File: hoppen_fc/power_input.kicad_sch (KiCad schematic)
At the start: 0 parts

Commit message: power input/generation reworked
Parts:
- added C54: 1u 50V, 0_capacitor_smd:C_0603_1608Metric, symbol Device:C
- added C55: 2u2, 0_capacitor_smd:C_0603_1608Metric, symbol Device:C
- added C57: 100n, 0_capacitor_smd:C_0402_1005Metric, symbol Device:C
- added D10: SMBJ51CD-M3/H, Diode_SMD:D_SMB, symbol 0_diodes:SMBJ51CD-M3/H
- added J4: XT30_MALE, 0_connectors:XT30PW-M, symbol 0_connectors:Conn_01x02_Mounting
- added Q2: NMOS, 0_transistors:DFN-8, symbol Simulation_SPICE:NMOS
- added U10: LM74700, 0_power:SOT-23-6, symbol 0_power:LM74700
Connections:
- new net: C54.2, U10.1 (VCAP)
- new net: Q2.2 (G), U10.5 (GATE)
- new net +BAT: C54.1, C57.1, D10.2 (A2), J4.2 (Pin_2), Q2.3 (S), U10.3 (EN), U10.6 (ANODE)
- new net +BAT_PROT: C55.1, Q2.1 (D), U10.4 (CATHODE)
- new net GND: C55.2, C57.2, D10.1 (A1), J4.1 (Pin_1), U10.2 (GND)
- no-connect marks 0 -> 2
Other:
- note added: "INPUT VOLTAGE MINIMUM 2S MAXIMUM 6S"
- note added: "POWER CONNECTOR AND PROTECTION"
- company: (none) -> Hoppen
- title: (none) -> Power Input

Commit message: finished routing, starting doublechecking and componenting
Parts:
- removed C55: 2u2, 0_capacitor_smd:C_0603_1608Metric, symbol Device:C
- added C64, C65, C66: 10u, 0_capacitor_smd:C_0805_2012Metric, symbol Device:C
- C54: value 1u 50V -> 1u
- Q2: LCSC (none) -> C467174
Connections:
- net +BAT_PROT: now also C64.1, C65.1, C66.1
- net GND: now also C64.2, C65.2, C66.2

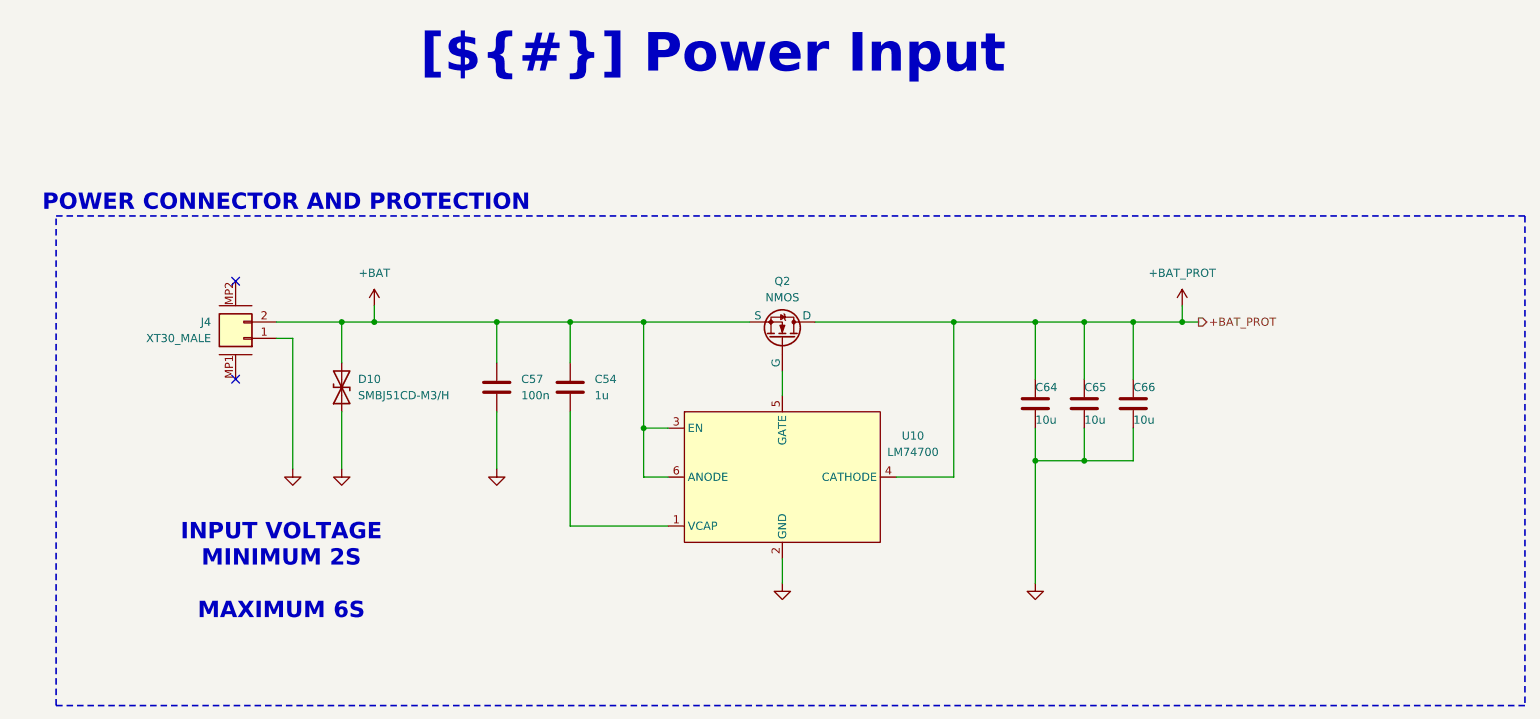
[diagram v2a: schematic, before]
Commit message: finished adding lcsc numbers
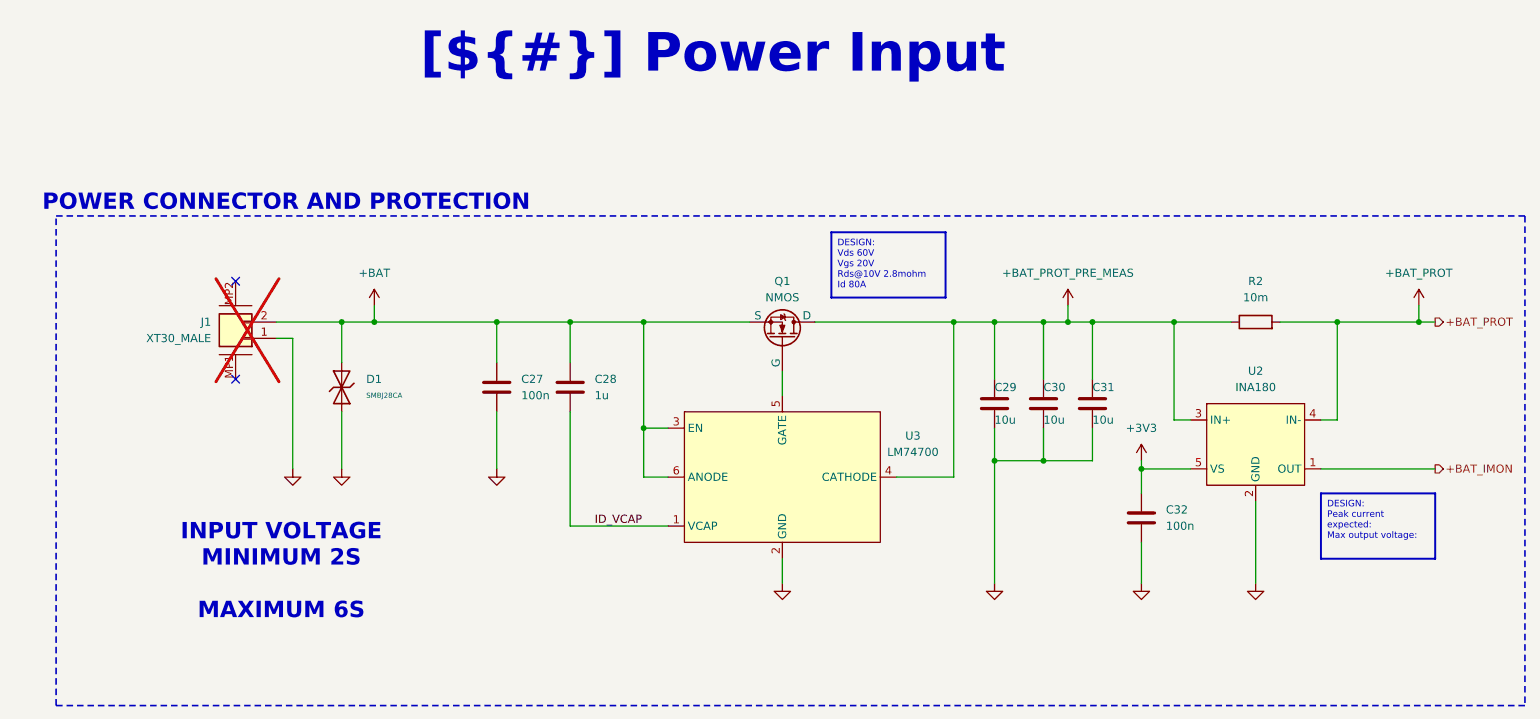
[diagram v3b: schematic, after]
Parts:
- removed D10: SMBJ51CD-M3/H, Diode_SMD:D_SMB, symbol 0_diodes:SMBJ51CD-M3/H
- added C32: 100n, 0_capacitor_smd:C_0402_1005Metric, symbol Device:C
- added D1: SMBJ28CA, PCM_JLCPCB:D_SMB, symbol PCM_JLCPCB-Diodes:TVS-Bi,SMBJ28CA
- added R2: 10m, Resistor_SMD:R_1206_3216Metric, symbol Device:R
- added U2: INA180, Package_TO_SOT_SMD:SOT-23-5, symbol 0_power:INA180
- C27: renamed from C57; LCSC (none) -> C307331
- C28: renamed from C54; LCSC (none) -> C15849
- J1: renamed from J4; now not fitted; now left out of the parts list
- renumbered C64 to C29, C65 to C30, C66 to C31, Q2 to Q1, U10 to U3
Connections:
- net +BAT: now also D1.2
- net +BAT_PROT: now also R2.2, U2.4 (IN-); no longer C29.1, C30.1, C31.1, Q1.1 (D), U3.4 (CATHODE)
- net GND: now also C32.2, D1.1, U2.2 (GND)
- net ID_VCAP: now reaches C28.2, U3.1 (VCAP)
- new net +3V3: C32.1, U2.5 (VS)
- new net +BAT_IMON: U2.1 (OUT)
- new net +BAT_PROT_PRE_MEAS: C29.1, C30.1, C31.1, Q1.1 (D), R2.1, U2.3 (IN+), U3.4 (CATHODE)
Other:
- moved on the sheet: C29, C30, C31

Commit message: ready for routing?
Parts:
- J1: now fitted
- U2: footprint Package_TO_SOT_SMD:SOT-23-5 -> 0_transceivers:SOT-23-5
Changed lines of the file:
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@@
 			)
 		)
-		(property "Footprint" "Package_TO_SOT_SMD:SOT-23-5"
+		(property "Footprint" "0_transceivers:SOT-23-5"
 			(at 224.79 60.96 0)
 			(effects
@@
 		(in_bom no)
 		(on_board yes)
-		(dnp yes)
+		(dnp no)
 		(fields_autoplaced yes)
 		(property "Reference" "J1"

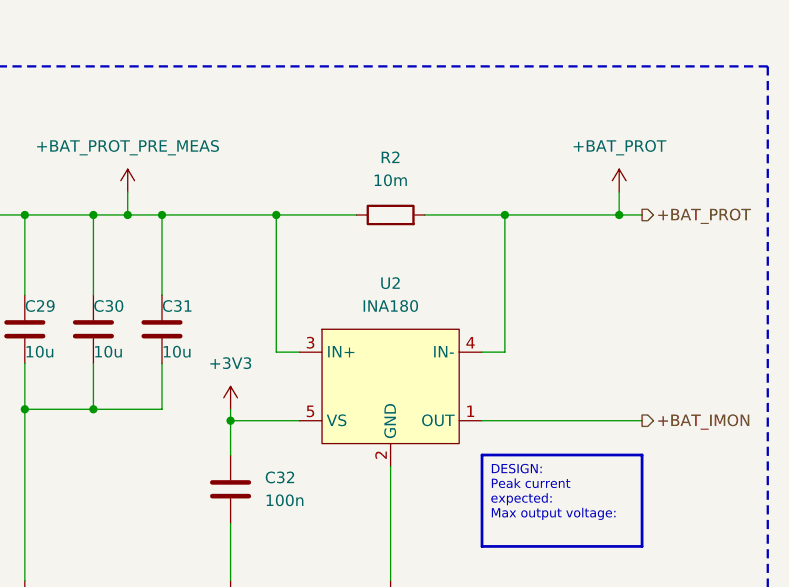
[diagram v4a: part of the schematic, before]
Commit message: routing and adding rf module
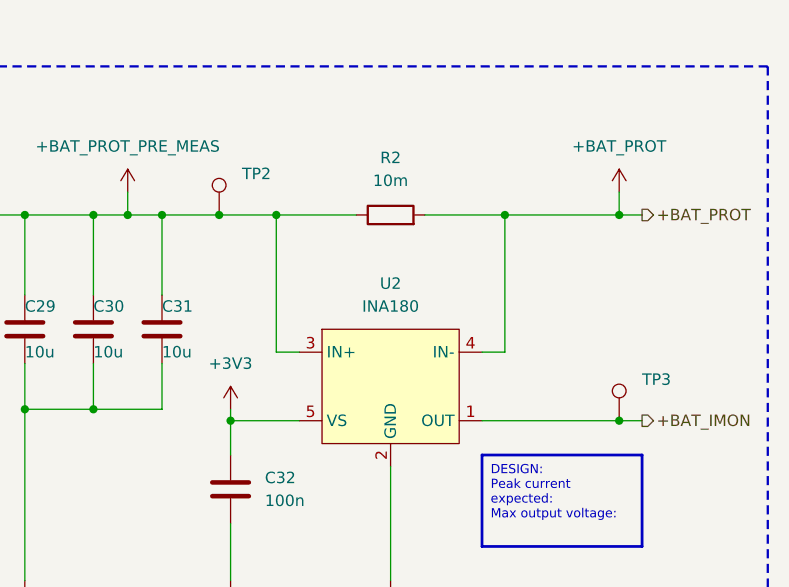
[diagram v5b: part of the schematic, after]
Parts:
- added TP2, TP3: TestPoint, TestPoint:TestPoint_Pad_1.0x1.0mm, symbol Connector:TestPoint
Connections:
- net +BAT_IMON: now also TP3.1
- net +BAT_PROT_PRE_MEAS: now also TP2.1
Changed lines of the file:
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@@
+	)
+	(junction
+		(at 205.74 67.31)
+		(diameter 0)
+		(color 0 0 0 0)
 	)
 	(junction
@@
 	)
 	(junction
+		(at 250.19 90.17)
+		(diameter 0)
+		(color 0 0 0 0)
+	)
+	(junction
 		(at 250.19 67.31)
 		(diameter 0)
@@
 	(wire
 		(pts
-			(xy 199.39 67.31) (xy 212.09 67.31)
+			(xy 199.39 67.31) (xy 205.74 67.31)
 		)
 		(stroke
@@
 	(wire
 		(pts
+			(xy 106.68 67.31) (xy 118.11 67.31)
+		)
+		(stroke
+			(width 0)
+			(type default)
+		)
+	)
+	(wire
+		(pts
 			(xy 87.63 67.31) (xy 87.63 64.77)
 		)
@@
 	(wire
 		(pts
-			(xy 234.95 90.17) (xy 252.73 90.17)
+			(xy 234.95 90.17) (xy 250.19 90.17)
+		)
+		(stroke
+			(width 0)
+			(type default)
+		)
+	)
+	(wire
+		(pts
+			(xy 250.19 90.17) (xy 252.73 90.17)
 		)
 		(stroke
@@
 	(wire
 		(pts
+			(xy 205.74 67.31) (xy 212.09 67.31)
+		)
+		(stroke
+			(width 0)
+			(type default)
+		)
+	)
+	(wire
+		(pts
 			(xy 212.09 67.31) (xy 220.98 67.31)
 		)
@@
 		(pts
 			(xy 237.49 67.31) (xy 250.19 67.31)
-		)
-		(stroke
-			(width 0)
-			(type default)
-		)
-	)
-	(wire
-		(pts
-			(xy 106.68 67.31) (xy 118.11 67.31)
 		)
 		(stroke
@@
 			)
 			(justify left)
+		)
+	)
+	(symbol
+		(lib_id "Connector:TestPoint")
+		(at 205.74 67.31 0)
+		(unit 1)
+		(exclude_from_sim no)
+		(in_bom yes)
+		(on_board yes)
+		(dnp no)
+		(fields_autoplaced yes)
+		(property "Reference" "TP2"
+			(at 208.28 62.7379 0)
+			(effects
+				(font
+					(size 1.27 1.27)
+				)
+				(justify left)
+			)
+		)
+		(property "Value" "TestPoint"
+			(at 208.28 65.2779 0)
+			(effects
+				(font
+					(size 1.27 1.27)
+				)
+				(justify left)
+				(hide yes)
+			)
+		)
+		(property "Footprint" "TestPoint:TestPoint_Pad_1.0x1.0mm"
+			(at 210.82 67.31 0)
+			(effects
+				(font
+					(size 1.27 1.27)
+				)
+				(hide yes)
+			)
+		)
+		(property "Datasheet" "~"
+			(at 210.82 67.31 0)
+			(effects
+				(font
+					(size 1.27 1.27)
+				)
+				(hide yes)
+			)
+		)
+		(property "Description" "test point"
+			(at 205.74 67.31 0)
+			(effects
+				(font
+					(size 1.27 1.27)
+				)
+				(hide yes)
+			)
+		)
+		(pin "1"
+		)
+		(instances
+			(project "hoppen_fc"
+				(path "/abe950a1-9eef-4508-9fd4-31d3e723e029/c85454e5-a89e-41eb-a5ed-71b4fc4cf13a/45aa82bb-5d0c-4be2-bfbe-f6adc776653e"
+					(reference "TP2")
+					(unit 1)
+				)
+			)
 		)
 	)
@@
 					(unit 1)
 				)
+			)
+		)
+	)
+	(symbol
+		(lib_id "Connector:TestPoint")
+		(at 250.19 90.17 0)
+		(unit 1)
+		(exclude_from_sim no)
+		(in_bom yes)
+		(on_board yes)
+		(dnp no)
+		(fields_autoplaced yes)
+		(property "Reference" "TP3"
+			(at 252.73 85.5979 0)
+			(effects
+				(font
+					(size 1.27 1.27)
+				)
+				(justify left)
+			)
+		)
+		(property "Value" "TestPoint"
+			(at 252.73 88.1379 0)
+			(effects
+				(font
+					(size 1.27 1.27)
+				)
+				(justify left)
+				(hide yes)
+			)
+		)
+		(property "Footprint" "TestPoint:TestPoint_Pad_1.0x1.0mm"
+			(at 255.27 90.17 0)
+			(effects
+				(font
+					(size 1.27 1.27)
+				)
+				(hide yes)
+			)
+		)
+		(property "Datasheet" "~"
+			(at 255.27 90.17 0)
+			(effects
+				(font
+					(size 1.27 1.27)
+				)
+				(hide yes)
+			)
+		)
+		(property "Description" "test point"
+			(at 250.19 90.17 0)
+			(effects
+				(font
+					(size 1.27 1.27)
+				)
+				(hide yes)
+			)
+		)
+		(pin "1"
+		)
+		(instances
+			(project "hoppen_fc"
+				(path "/abe950a1-9eef-4508-9fd4-31d3e723e029/c85454e5-a89e-41eb-a5ed-71b4fc4cf13a/45aa82bb-5d0c-4be2-bfbe-f6adc776653e"
+					(reference "TP3")
+					(unit 1)
+				)

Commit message: sync
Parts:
- J1: value XT30_MALE -> XT30 M
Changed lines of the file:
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@@
 			)
 		)
-		(property "Value" "XT30_MALE"
+		(property "Value" "XT30 M"
 			(at 62.23 69.8499 0)
 			(effects

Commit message: bump
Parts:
- renumbered TP2 to TP1, TP3 to TP2
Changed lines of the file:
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@@
 		(dnp no)
 		(fields_autoplaced yes)
-		(property "Reference" "TP2"
+		(property "Reference" "TP1"
 			(at 208.28 62.7379 0)
 			(effects
@@
 			(project "hoppen_fc"
 				(path "/abe950a1-9eef-4508-9fd4-31d3e723e029/c85454e5-a89e-41eb-a5ed-71b4fc4cf13a/45aa82bb-5d0c-4be2-bfbe-f6adc776653e"
-					(reference "TP2")
+					(reference "TP1")
 					(unit 1)
 				)
@@
 		(dnp no)
 		(fields_autoplaced yes)
-		(property "Reference" "TP3"
+		(property "Reference" "TP2"
 			(at 252.73 85.5979 0)
 			(effects
@@
 			(project "hoppen_fc"
 				(path "/abe950a1-9eef-4508-9fd4-31d3e723e029/c85454e5-a89e-41eb-a5ed-71b4fc4cf13a/45aa82bb-5d0c-4be2-bfbe-f6adc776653e"
-					(reference "TP3")
-					(unit 1)
-				)
+					(reference "TP2")
+					(unit 1)
+				)

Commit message: bump
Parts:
- removed C27: 100n, 0_capacitor_smd:C_0402_1005Metric, symbol Device:C
- removed C28: 1u, 0_capacitor_smd:C_0603_1608Metric, symbol Device:C
- removed C31: 10u, 0_capacitor_smd:C_0805_2012Metric, symbol Device:C
- removed D1: SMBJ28CA, PCM_JLCPCB:D_SMB, symbol PCM_JLCPCB-Diodes:TVS-Bi,SMBJ28CA
- added C30: 10u, 0_capacitor_smd:C_0805_2012Metric, symbol Device:C
- added D1: SMBJ28CA, Diode_SMD:D_SMB, symbol Device:D_TVS
- renumbered C29 to C31, C30 to C32, C32 to C33, TP1 to TP2, TP2 to TP3, U2 to U3, U3 to U4
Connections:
- net +BAT: now also C30.1, D1.2 (A2)
- net GND: now also D1.1 (A1)
- net ID_VCAP: now also C30.2
- net ID_GATE: now reaches Q1.2 (G), U4.5 (GATE)
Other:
- moved on the sheet: C31, C32
